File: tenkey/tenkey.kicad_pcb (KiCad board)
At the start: 2 copper layers, 78.7 x 97.8 mm, 53 parts, among them J1 USB, P1 SCK, P2 MISO, P3 MOSI, P4 RESET, P5 5V, P6 GND, SW0:0 NUM_0, SW0:2 DOT, SW1 RESET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

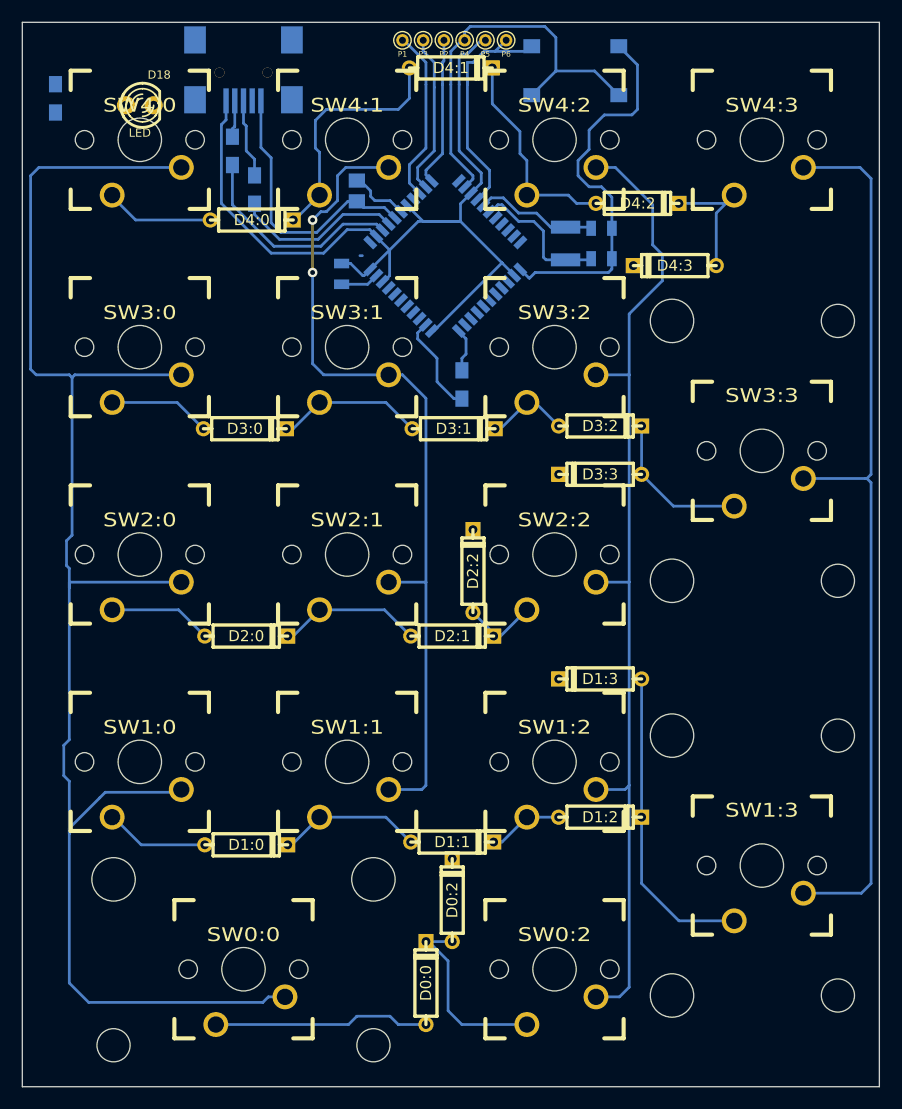
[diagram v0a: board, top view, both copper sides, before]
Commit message: PCB routing done, needs to check and reconcile footprints before ordering components
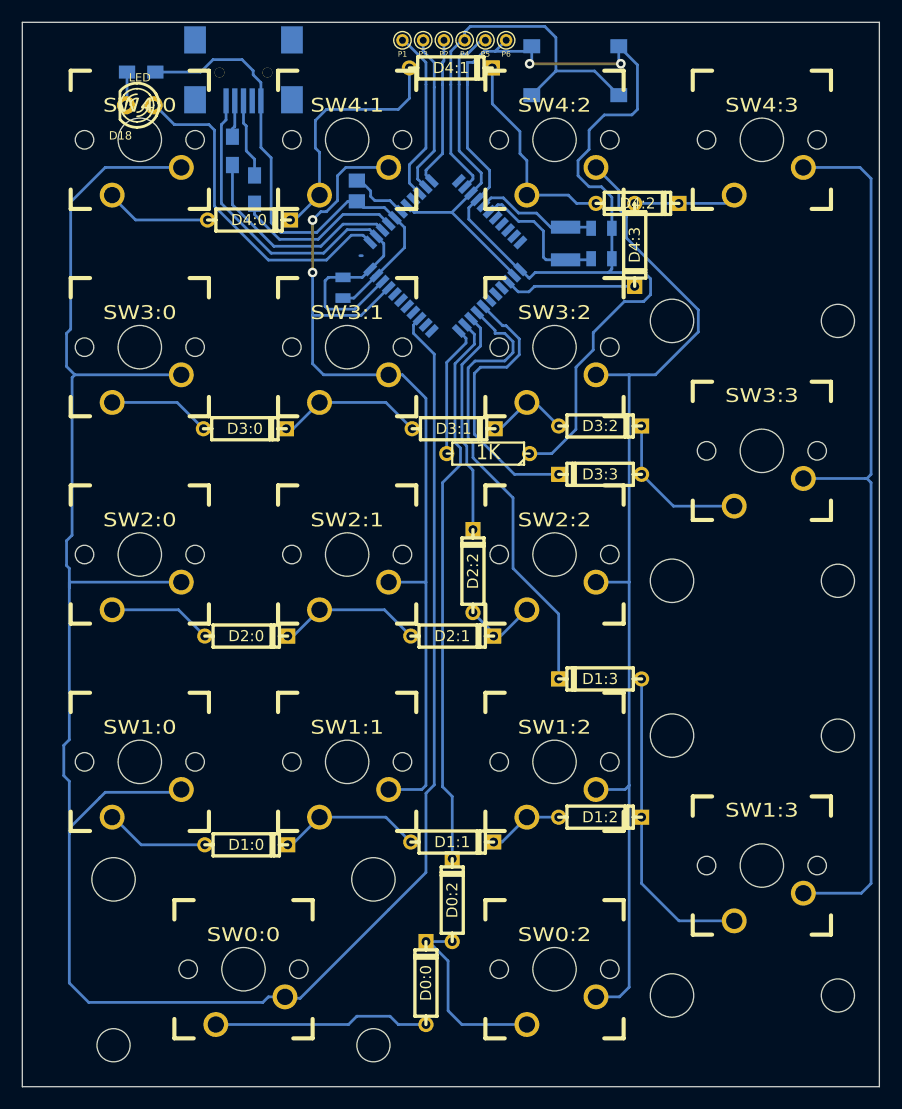
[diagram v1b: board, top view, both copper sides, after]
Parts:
- R5: footprint Resistors_SMD:Resistor_SMD0805_HandSoldering -> Discret:R3; moved to F.Cu
- moved R1 8.24 mm to (111.3, 64.9), turned to 0 degrees
- moved R5 6.79 mm to (143.1, 99.9), turned to 180 degrees
- moved D4:3 4.15 mm to (156.6, 80.8), turned to 270 degrees
- moved C1 1.28 mm to (129.8, 84.7)
- moved D4:0 0.25 mm to (121.2, 78.5)
- turned D18 to 180 degrees
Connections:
- U1 pad 1: Net-(U1-Pad1) -> /LED_A
- U1 pad 25: Net-(U1-Pad25) -> /ROW4
- U1 pad 29: Net-(U1-Pad29) -> /ROW3
- U1 pad 30: Net-(U1-Pad30) -> /ROW1
- U1 pad 31: Net-(U1-Pad31) -> /ROW2
- U1 pad 32: Net-(U1-Pad32) -> /ROW0
- U1 pad 36: Net-(U1-Pad36) -> /COL0
- U1 pad 41: Net-(U1-Pad41) -> /COL1
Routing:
- net /COL0: track 146.4 -> 208.2 mm
- net GND: track 95.6 -> 154.0 mm, vias 0 -> 2
- net /ROW0: track 0.00 -> 51.4 mm
- net /ROW1: track 0.00 -> 42.3 mm
- net /LED_A: track 0.00 -> 31.1 mm
- net /ROW3: track 0.00 -> 25.7 mm
- net /ROW2: track 0.00 -> 20.9 mm
- net /ROW4: track 0.00 -> 12.4 mm
- net /+5V: track 87.0 -> 76.7 mm
- net Net-(R5-Pad2): track 4.05 -> 12.3 mm
- net /COL1: track 79.1 -> 87.1 mm
- net /COL2: track 92.9 -> 96.0 mm
- net Net-(D18-Pad2): track 0.00 -> 3.09 mm
- net Net-(D4:2-Pad2): track 10.4 -> 8.38 mm

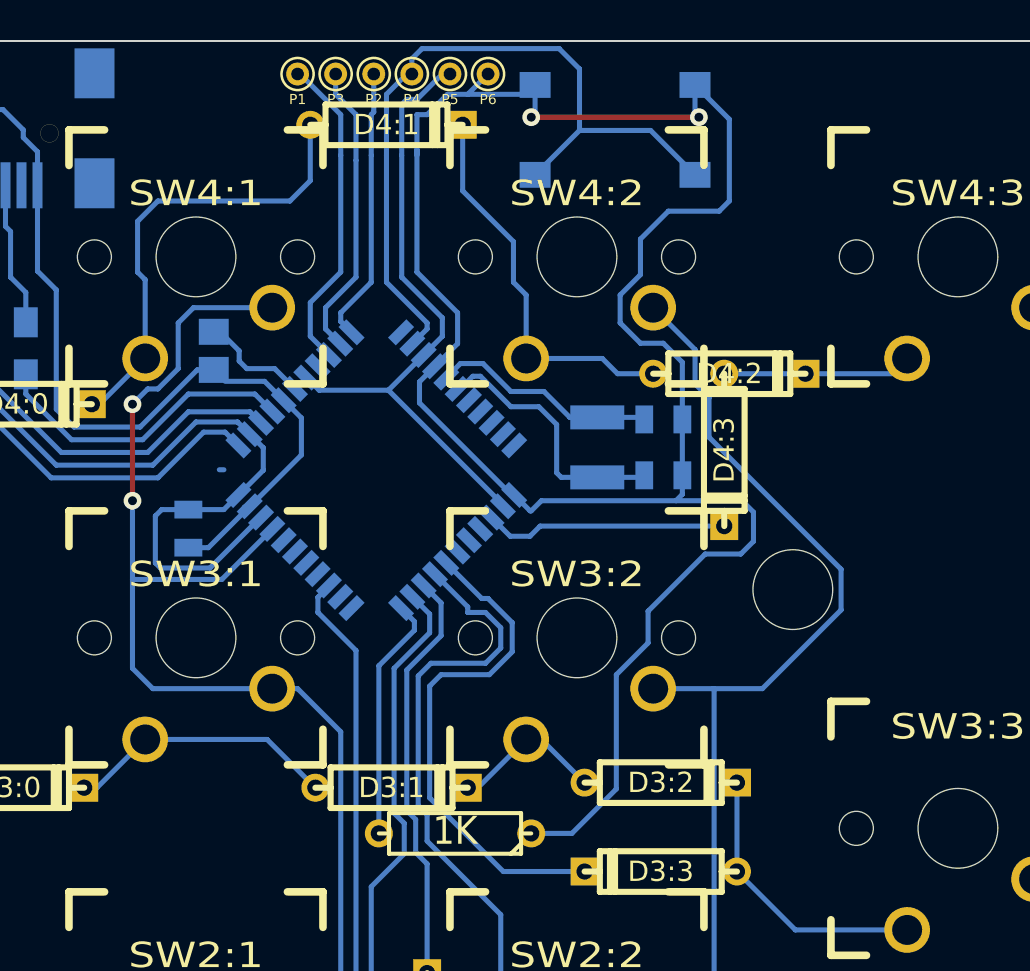
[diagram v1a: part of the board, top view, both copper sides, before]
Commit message: larger vias and moved diodes out of area reserved for switches
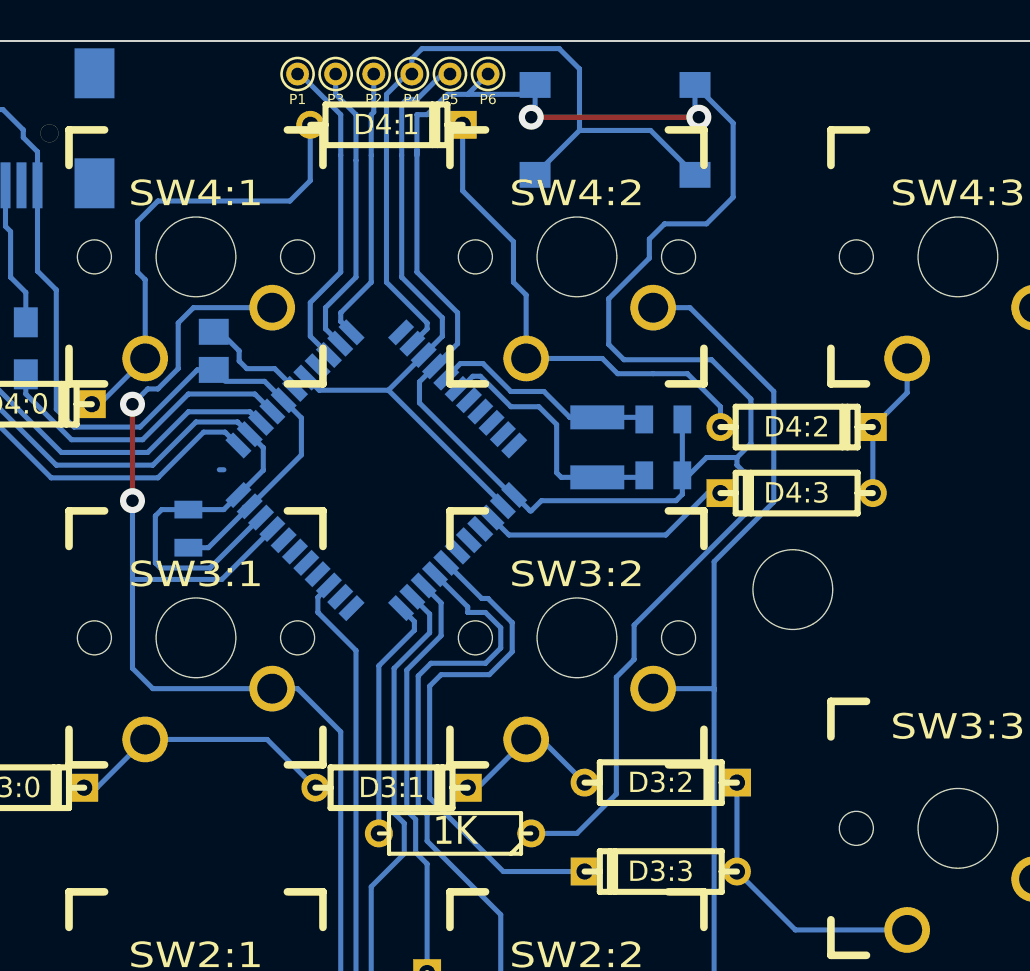
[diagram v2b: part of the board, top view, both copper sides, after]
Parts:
- moved D4:2 4.29 mm to (160.2, 79.6)
- moved D4:3 4.21 mm to (160.2, 82.9), turned to 180 degrees
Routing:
- net GND: track 154.0 -> 160.9 mm
- net Net-(D4:1-Pad2): track 19.7 -> 24.7 mm
- net /COL2: track 96.0 -> 92.9 mm
- net Net-(D4:2-Pad2): track 8.38 -> 7.44 mm
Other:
- net class Default: via_dia 0.889 -> 1.25

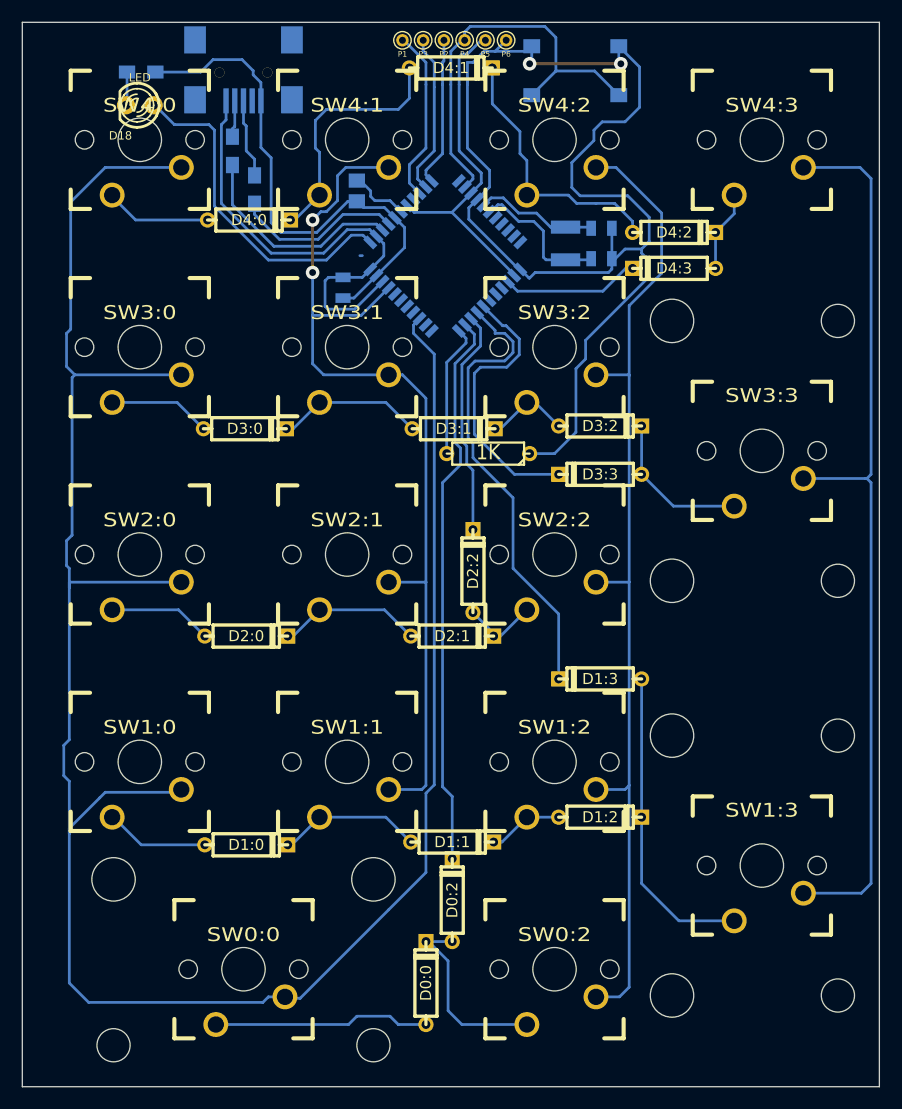
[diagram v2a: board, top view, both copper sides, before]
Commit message: connected ROW2 and ROW3 to ATMEGA32U4 and added mounting holes
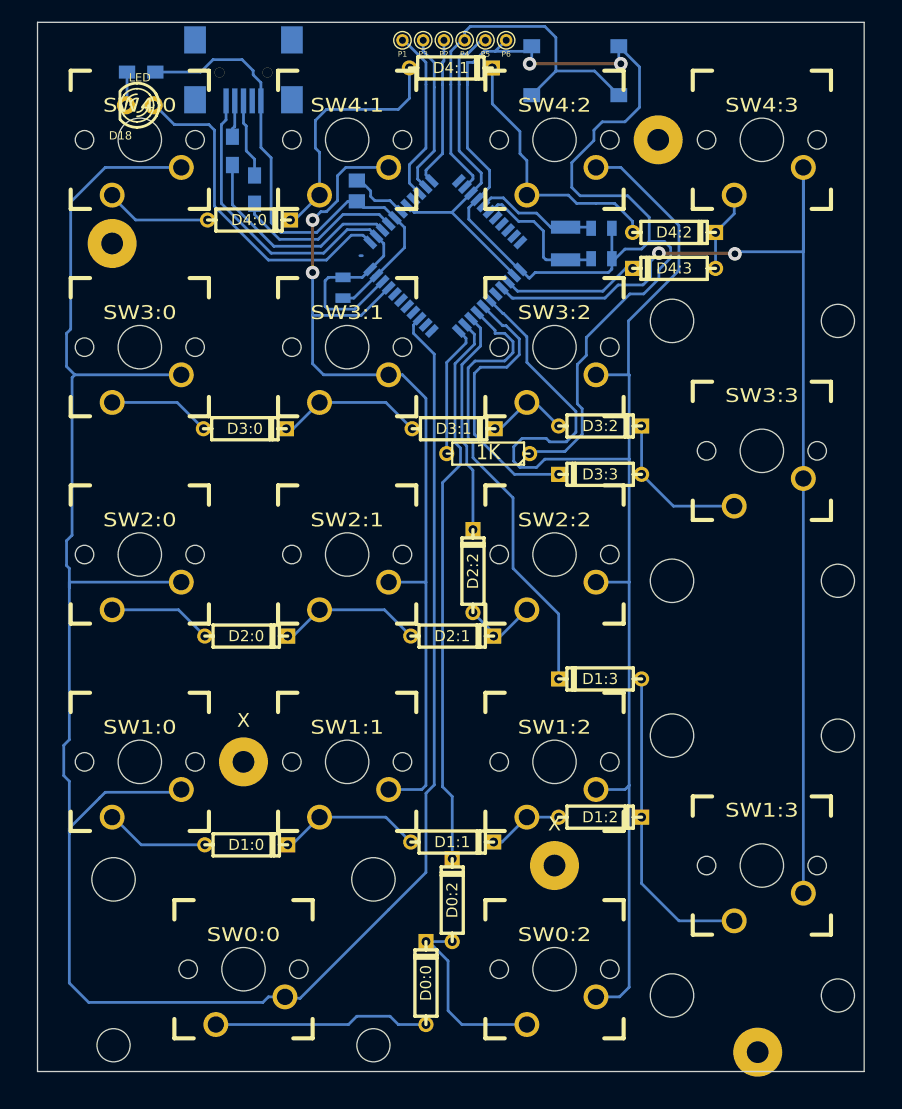
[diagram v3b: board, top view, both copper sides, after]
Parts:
- added ?: SolderWirePad_single_2mmDrill, Wire_Pads:SolderWirePad_single_2mmDrill, F.Cu at (108.6, 80.6)
- added ?: SolderWirePad_single_2mmDrill, Wire_Pads:SolderWirePad_single_2mmDrill, F.Cu at (158.8, 71.1)
- added ?: SolderWirePad_single_2mmDrill, Wire_Pads:SolderWirePad_single_2mmDrill, F.Cu at (167.9, 154.9)
- added X: SolderWirePad_single_2mmDrill, Wire_Pads:SolderWirePad_single_2mmDrill, F.Cu at (149.2, 137.8)
- added X: SolderWirePad_single_2mmDrill, Wire_Pads:SolderWirePad_single_2mmDrill, F.Cu at (120.7, 128.3)
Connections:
- U1 pad 26: Net-(U1-Pad26) -> /COL3
- U1 pad 28: Net-(U1-Pad28) -> /COL2
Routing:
- net /COL2: track 92.9 -> 128.9 mm
- net /COL3: track 84.2 -> 105.2 mm, vias 0 -> 2
- net GND: track 160.9 -> 165.4 mm
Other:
- board size 78.7 x 97.8 mm -> 75.9 x 96.4 mm

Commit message: moved some close traces
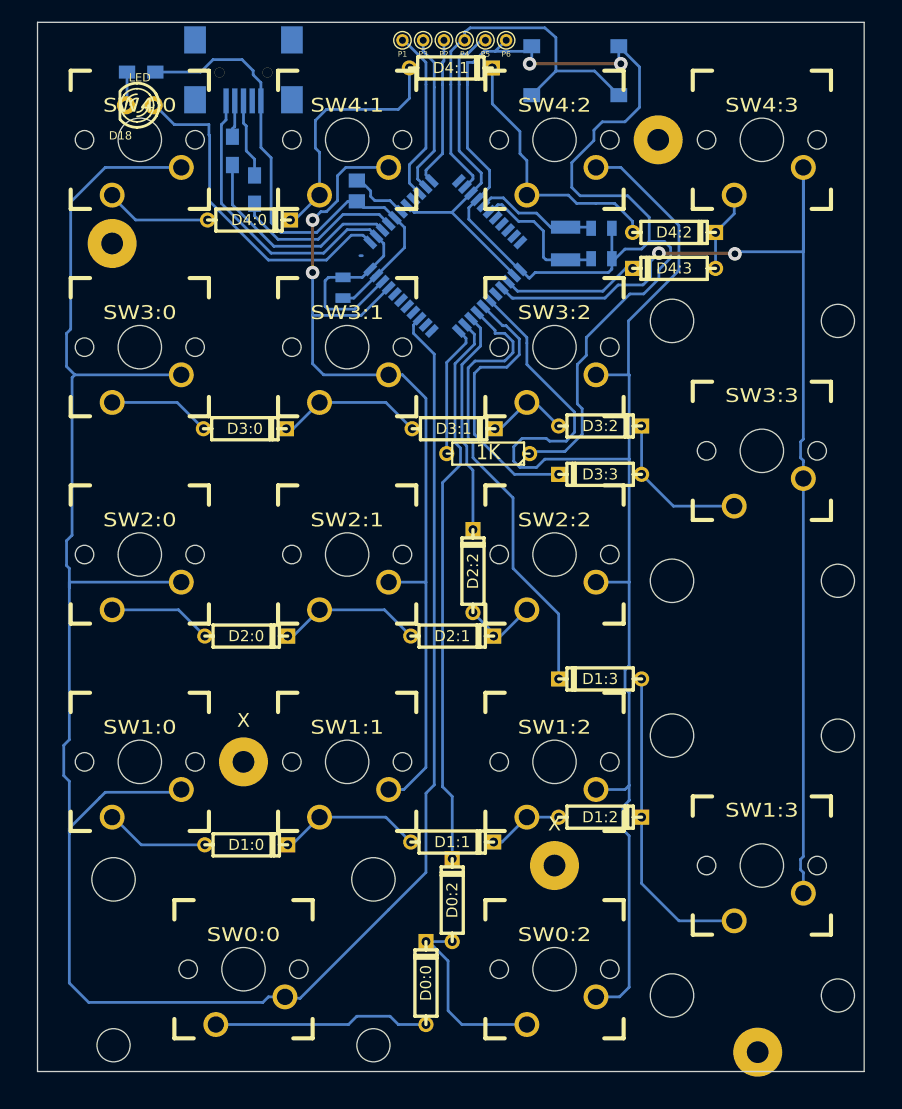
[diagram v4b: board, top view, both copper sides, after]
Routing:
- net /COL1: track 87.1 -> 86.2 mm
- net /COL2: track 128.9 -> 129.5 mm
